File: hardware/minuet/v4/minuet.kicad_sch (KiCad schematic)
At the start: 42 parts, among them J1 B2P-VH-B, J2 B2B-XH-A, J3 B2B-XH-A, J4 PPPC082LFBN-RC, J5 B2B-XH-A, Q1 MMBT3904, U1 TSOP39238, U2 LMV331IDCK

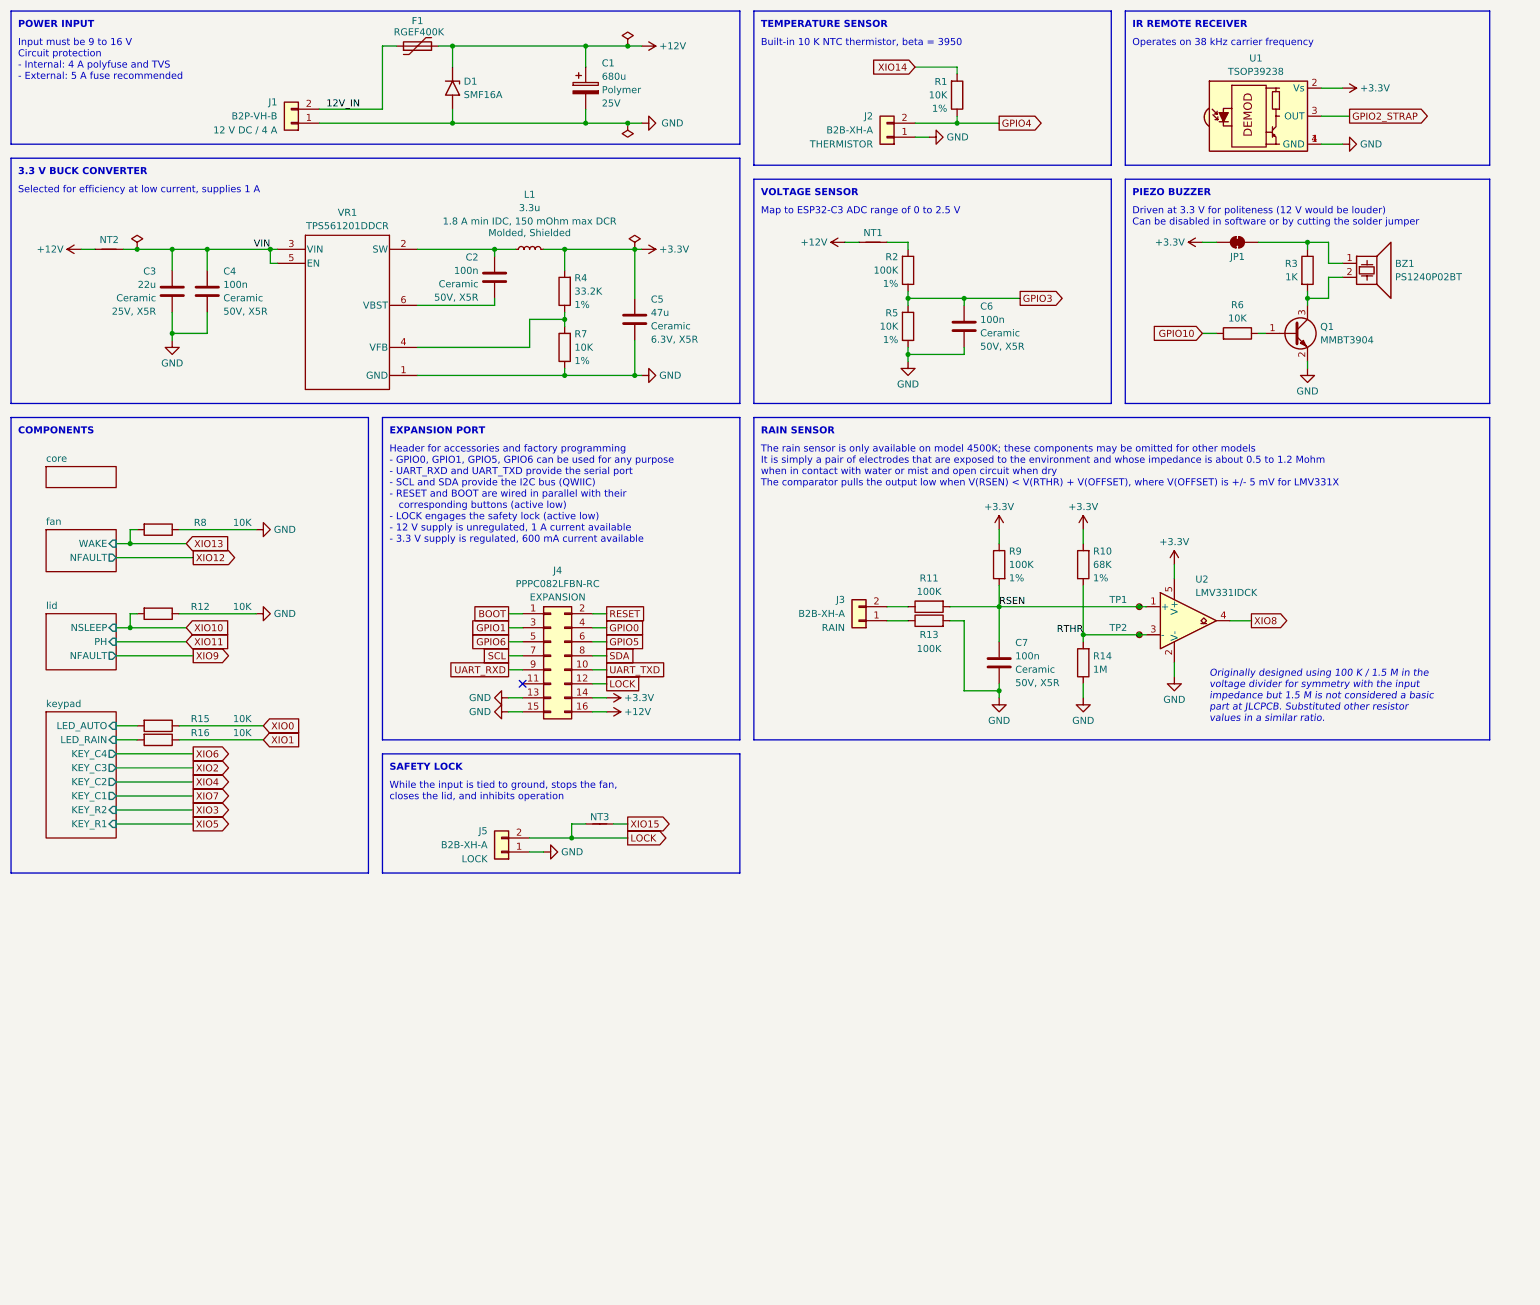
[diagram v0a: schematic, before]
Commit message: First draft of Minuet v4 fan controller board
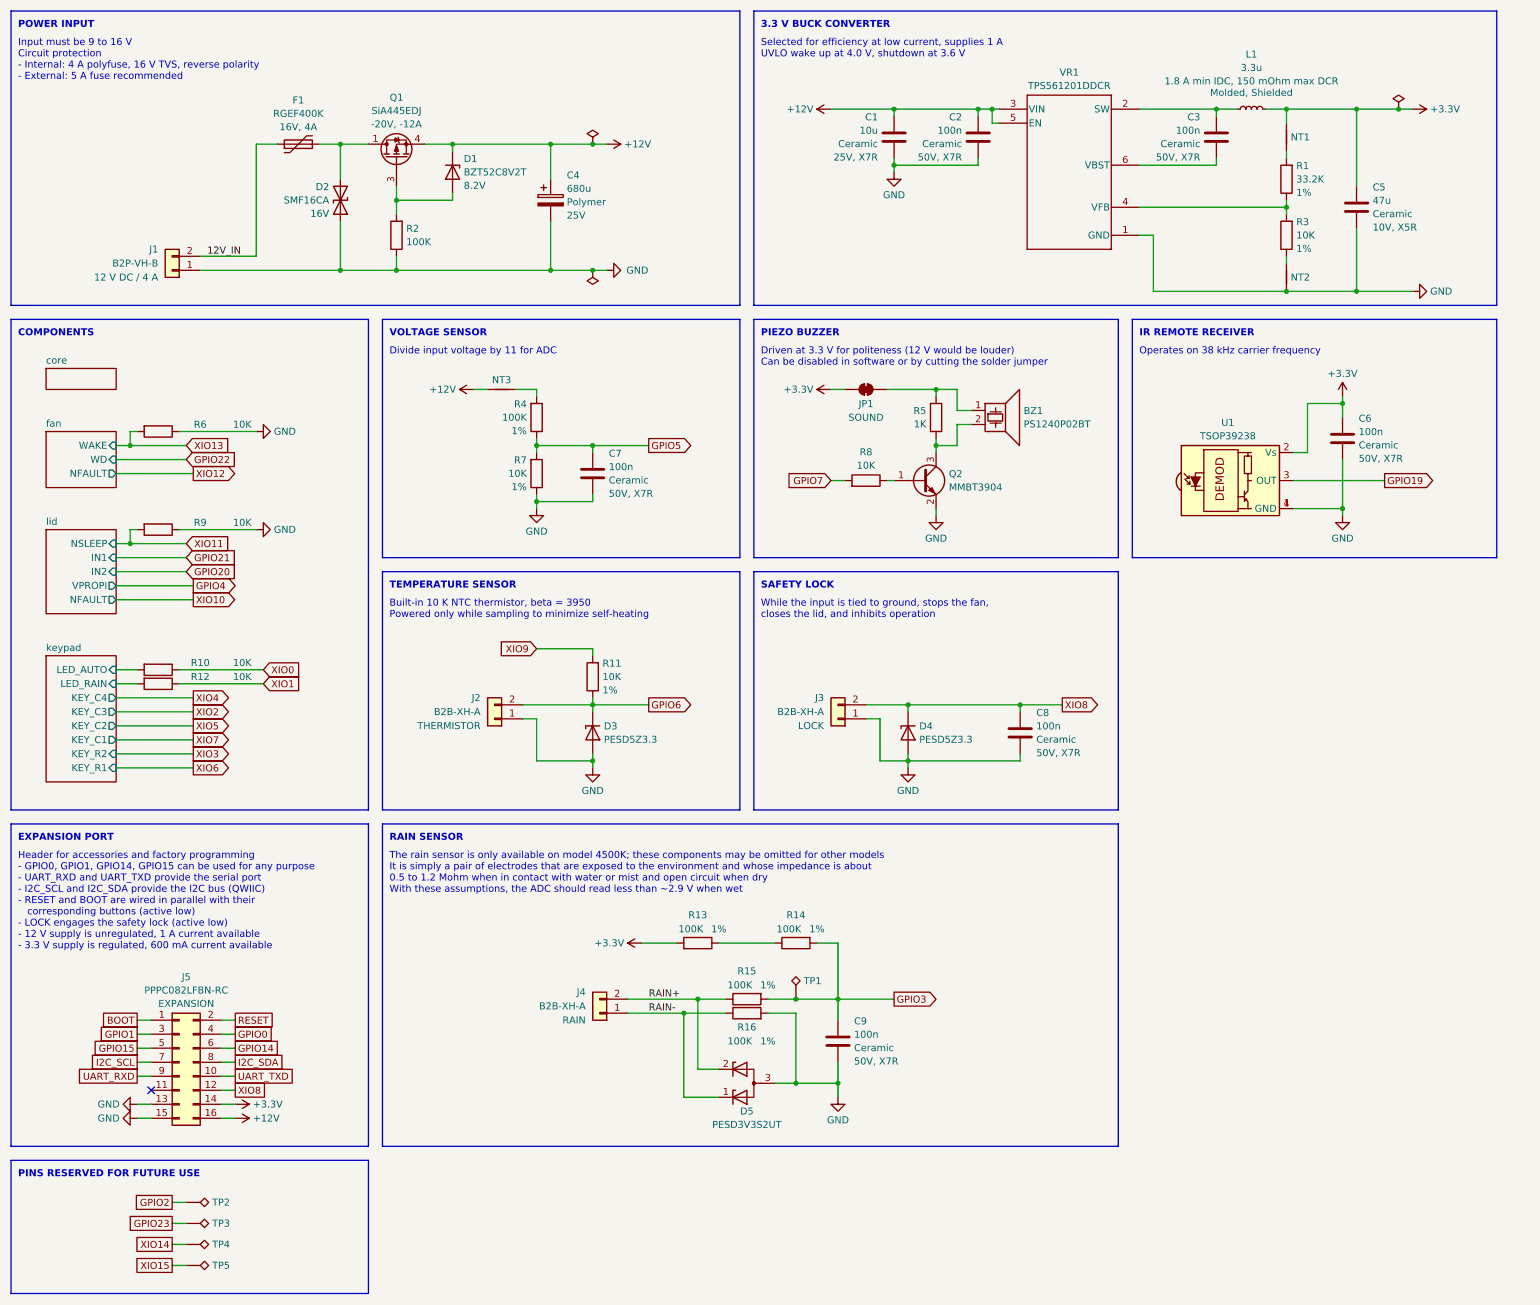
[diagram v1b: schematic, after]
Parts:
- removed C3: 22u, Capacitor_SMD:C_0805_2012Metric, symbol Device:C
- removed D1: SMF16A, Diode_SMD:D_SMF, symbol Diode:SMF16A
- removed NT3: NetTie_2, Generic:NetTie-2_SMD_Pad0.2mm, symbol Device:NetTie_2
- removed R10: 68K, Resistor_SMD:R_0603_1608Metric, symbol Device:R
- removed R14: 1M, Resistor_SMD:R_0603_1608Metric, symbol Device:R
- removed TP1, TP2: TestPoint_Small, TestPoint:TestPoint_Pad_D1.0mm, symbol Connector:TestPoint_Small
- removed U2: LMV331IDCK, Package_TO_SOT_SMD:SOT-353_SC-70-5, symbol Comparator:LMV331
- added C1: 10u, Capacitor_SMD:C_1210_3225Metric, symbol Device:C
- added C6, C8: 100n, Capacitor_SMD:C_0603_1608Metric, symbol Device:C
- added D1: BZT52C8V2T, Diode_SMD:D_SOD-523, symbol Device:D_Zener
- added D2: SMF16CA, Diode_SMD:D_SMF, symbol Device:D_TVS
- added D3, D4: PESD5Z3.3, Diode_SMD:D_SOD-523, symbol Device:D_Zener
- added D5: PESD3V3S2UT, Package_TO_SOT_SMD:SOT-23, symbol Device:D_Zener_Dual_CommonAnode_KKA_Parallel
- added NT1: NetTie_2, Generic:NetTie-2_SMD_Pad0.2mm, symbol Device:NetTie_2
- added Q1: SiA445EDJ, Package_TO_SOT_SMD:Vishay_PowerPAK_SC70-6L_Single, symbol Transistor_FET:SiA453EDJ
- added R13, R2: 100K, Resistor_SMD:R_0603_1608Metric, symbol Device:R
- added TP1, TP2, TP3, TP4, TP5: TestPoint_Alt, TestPoint:TestPoint_Pad_D1.0mm, symbol Connector:TestPoint_Alt
- C2: renamed from C4; Rating 50V, X5R -> 50V, X7R
- C3: renamed from C2; Rating 50V, X5R -> 50V, X7R
- C5: footprint Capacitor_SMD:C_0805_2012Metric -> Capacitor_SMD:C_1206_3216Metric; LCSC C16780 -> C96123; Rating 6.3V, X5R -> 10V, X5R
- C7: renamed from C6; Rating 50V, X5R -> 50V, X7R
- C9: renamed from C7; Rating 50V, X5R -> 50V, X7R
- F1: Rating (none) -> 16V, 4A
- JP1: Label (none) -> SOUND
- NT2: footprint Generic:NetTie-2_SMD_Pad1.0mm -> Generic:NetTie-2_SMD_Pad0.2mm
- R10: renamed from R15; Rating (none) -> 1%
- R12: renamed from R16; Rating (none) -> 1%
- R15: renamed from R11; Rating (none) -> 1%
- R16: renamed from R13; Rating (none) -> 1%
- R5: renamed from R3; Rating (none) -> 1%
- R6: renamed from R8; Rating (none) -> 1%
- R8: renamed from R6; Rating (none) -> 1%
- R9: renamed from R12; Rating (none) -> 1%
- renumbered C1 to C4, J5 to J3, J3 to J4, J4 to J5, NT1 to NT3, Q1 to Q2, R4 to R1, R1 to R11, R9 to R14, R7 to R3, R2 to R4, R5 to R7
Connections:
- net LOCK is gone; now on net XIO8: J3.2 (Pin_2), J5.12 (Pin_12)
- net RSEN is gone; now on net GPIO3: C9.1, R14.2, R15.2
- net +12V: now also C2.1, VR1.3 (VIN), VR1.5 (EN), C1.1, D1.1 (K), Q1.4 (S); no longer F1.2, NT2.1
- net +3.3V: now also C6.1, NT1.2, R13.2; no longer R1.2, R14.1
- net GND: now also NT2.1, C1.2, C6.2, C8.2, D2.1 (A1), D3.2 (A), D4.2 (A), D5.3 (A), R2.1; no longer R3.1
- net GPIO3: now also TP1.1; no longer C7.1, R4.1, R7.2
- net GPIO4: no longer J2.2 (Pin_2), R11.1
- net GPIO5: now also C7.1, R4.1, R7.2; no longer J5.6 (Pin_6)
- net GPIO6: now also J2.2 (Pin_2), R11.1, D3.1 (K); no longer J5.5 (Pin_5)
- net XIO10: no longer R9.2
- net XIO11: now also R9.2
- net XIO14: now also TP4.1; no longer R11.2
- net XIO15: now also TP5.1
- net XIO8: now also C8.1, D4.1 (K)
- net XIO9: now also R11.2
- net RAIN-: now reaches J4.1 (Pin_1), R16.1
- net RAIN-: now also D5.1 (K)
- net RAIN+: now reaches J4.2 (Pin_2), R15.1
- net RAIN+: now also D5.2 (K)
- net GPIO10 renamed GPIO7
- net GPIO2_STRAP renamed GPIO19
- net SCL renamed I2C_SCL
- net SDA renamed I2C_SDA
- removed net VIN: C2.1, NT2.2, VR1.3 (VIN), VR1.5 (EN)
- new net: R13.1, R14.1
- new net: D2.2 (A2), F1.2, Q1.1 (D)
- new net: D1.2 (A), Q1.3 (G), R2.2
- new net: NT1.1, R1.2
- new net: NT2.2, R3.1
- new net GPIO14: J5.6 (Pin_6)
- new net GPIO15: J5.5 (Pin_5)
- new net GPIO2: TP2.1
- new net GPIO23: TP3.1
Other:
- sheet fan ports: added WD; removed none
- sheet lid ports: added IN1, IN2, VPROPI; removed PH
- note added: "Built-in 10 K NTC thermistor, beta = 3950 Powered only while sampling to minimize self-heating"
- note added: "Divide input voltage by 11 for ADC"
- note added: "Header for accessories and factory programming - GPIO0, GPIO1, GPIO14, GPIO15 can be used for any purpose - UART_RXD and UART_TXD provide the serial port - I2C_SCL and I2C_SDA provide the I2C bus (QWIIC) - RESET and BOOT are wired in parallel with their corresponding buttons (active low) - LOCK engages the safety lock (active low) - 12 V supply is unregulated, 1 A current available - 3.3 V supply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"
- note added: "Input must be 9 to 16 V Circuit protection - Internal: 4 A polyfuse, 16 V TVS, reverse polarity - External: 5 A fuse recommended"
- note added: "PINS RESERVED FOR FUTURE USE"
- note added: "Selected for efficiency at low current, supplies 1 A UVLO wake up at 4.0 V, shutdown at 3.6 V"
- note added: "The rain sensor is only available on model 4500K; these components may be omitted for other models It is simply a pair of electrodes that are exposed to the environment and whose impedance is about 0.5 to 1.2 Mohm when in contact with water or mist and open circuit when dry With these assumptions, the ADC should read less than ~2.9 V when wet"
- note removed: "Built-in 10 K NTC thermistor, beta = 3950"
- note removed: "Header for accessories and factory programming - GPIO0, GPIO1, GPIO5, GPIO6 can be used for any purpose - UART_RXD and UART_TXD provide the serial port - SCL and SDA provide the I2C bus (QWIIC) - RESET and BOOT are wired in parallel with their corresponding buttons (active low) - LOCK engages the safety lock (active low) - 12 V supply is unregulated, 1 A current available - 3.3 V supply is regula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"
- note removed: "Input must be 9 to 16 V Circuit protection - Internal: 4 A polyfuse and TVS - External: 5 A fuse recommended"
- note removed: "Map to ESP32-C3 ADC range of 0 to 2.5 V"
- note removed: "Originally designed using 100 K / 1.5 M in the voltage divider for symmetry with the input impedance but 1.5 M is not considered a basic part at JLCPCB. Substituted other resistor values in a similar ratio."
- note removed: "Selected for efficiency at low current, supplies 1 A"
- note removed: "The rain sensor is only available on model 4500K; these components may be omitted for other models It is simply a pair of electrodes that are exposed to the environment and whose impedance is about 0.5 to 1.2 Mohm when in contact with water or mist and open circuit when dry The comparator pulls the output low when V(RSEN) < V(RTHR) + V(OFFSET), where V(OFFSET) is +/- 5 mV for LMV331X"
- moved on the sheet: BZ1, C2, C3, C4, C5, C7, C9, F1, J1, J2, J3, J4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

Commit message: Second draft of Minuet v4 main board.
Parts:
- removed TP2: TestPoint_Alt, TestPoint:TestPoint_Pad_D1.0mm, symbol Connector:TestPoint_Alt
- added C9: 100n, Capacitor_SMD:C_0603_1608Metric, symbol Device:C
- added R13: 100K, Resistor_SMD:R_0603_1608Metric, symbol Device:R
- J5: FT Rotation Offset (none) -> 90; LCSC C2897409 -> C30734; LCSC_Alternative (none) -> C2897409
- Q1: FT Rotation Offset (none) -> 270
- U1: now not fitted
- renumbered C9 to C10, R13 to R14, R14 to R15, R15 to R16, R16 to R17, TP3 to TP2, TP4 to TP3, TP5 to TP4
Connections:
- net +3.3V: now also R13.2
- net GND: now also C9.2
- net GPIO2: now also C10.1, R15.2, R16.2, TP1.1
- net GPIO3: now also D3.1 (K), J2.2 (Pin_2), R11.1; no longer C10.1, R15.2, R16.2, TP1.1
- net GPIO6: now also J5.11 (Pin_11), C9.1, R13.1; no longer D3.1 (K), J2.2 (Pin_2), R11.1
- no-connect marks 1 -> 0
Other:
- note added: "ACCESSORY ID"
- note added: "Header for accessories and factory programming - GPIO0, GPIO1, GPIO14, GPIO15 can be used for any purpose - UART_RXD and UART_TXD provide the serial port - I2C_SCL and I2C_SDA provide the I2C bus (QWIIC) - RESET and BOOT are wired in parallel with their corresponding buttons (active low) - LOCK engages the safety lock (active low) - ACC_ID identifies the expansion port accessory - 12 V supply is 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"
- note added: "Identifies the expansion port accessory Refer to the design document for details"
- note removed: "Header for accessories and factory programming - GPIO0, GPIO1, GPIO14, GPIO15 can be used for any purpose - UART_RXD and UART_TXD provide the serial port - I2C_SCL and I2C_SDA provide the I2C bus (QWIIC) - RESET and BOOT are wired in parallel with their corresponding buttons (active low) - LOCK engages the safety lock (active low) - 12 V supply is unregulated, 1 A current available - 3.3 V supply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"
- moved on the sheet: TP2, TP3, TP4
